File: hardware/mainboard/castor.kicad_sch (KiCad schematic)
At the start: 46 parts, among them J116 OSC, Q1 MMBT3906, U3 TL074, U4 74LVC2G74, U5 MCP6001-OT, U6 TL074

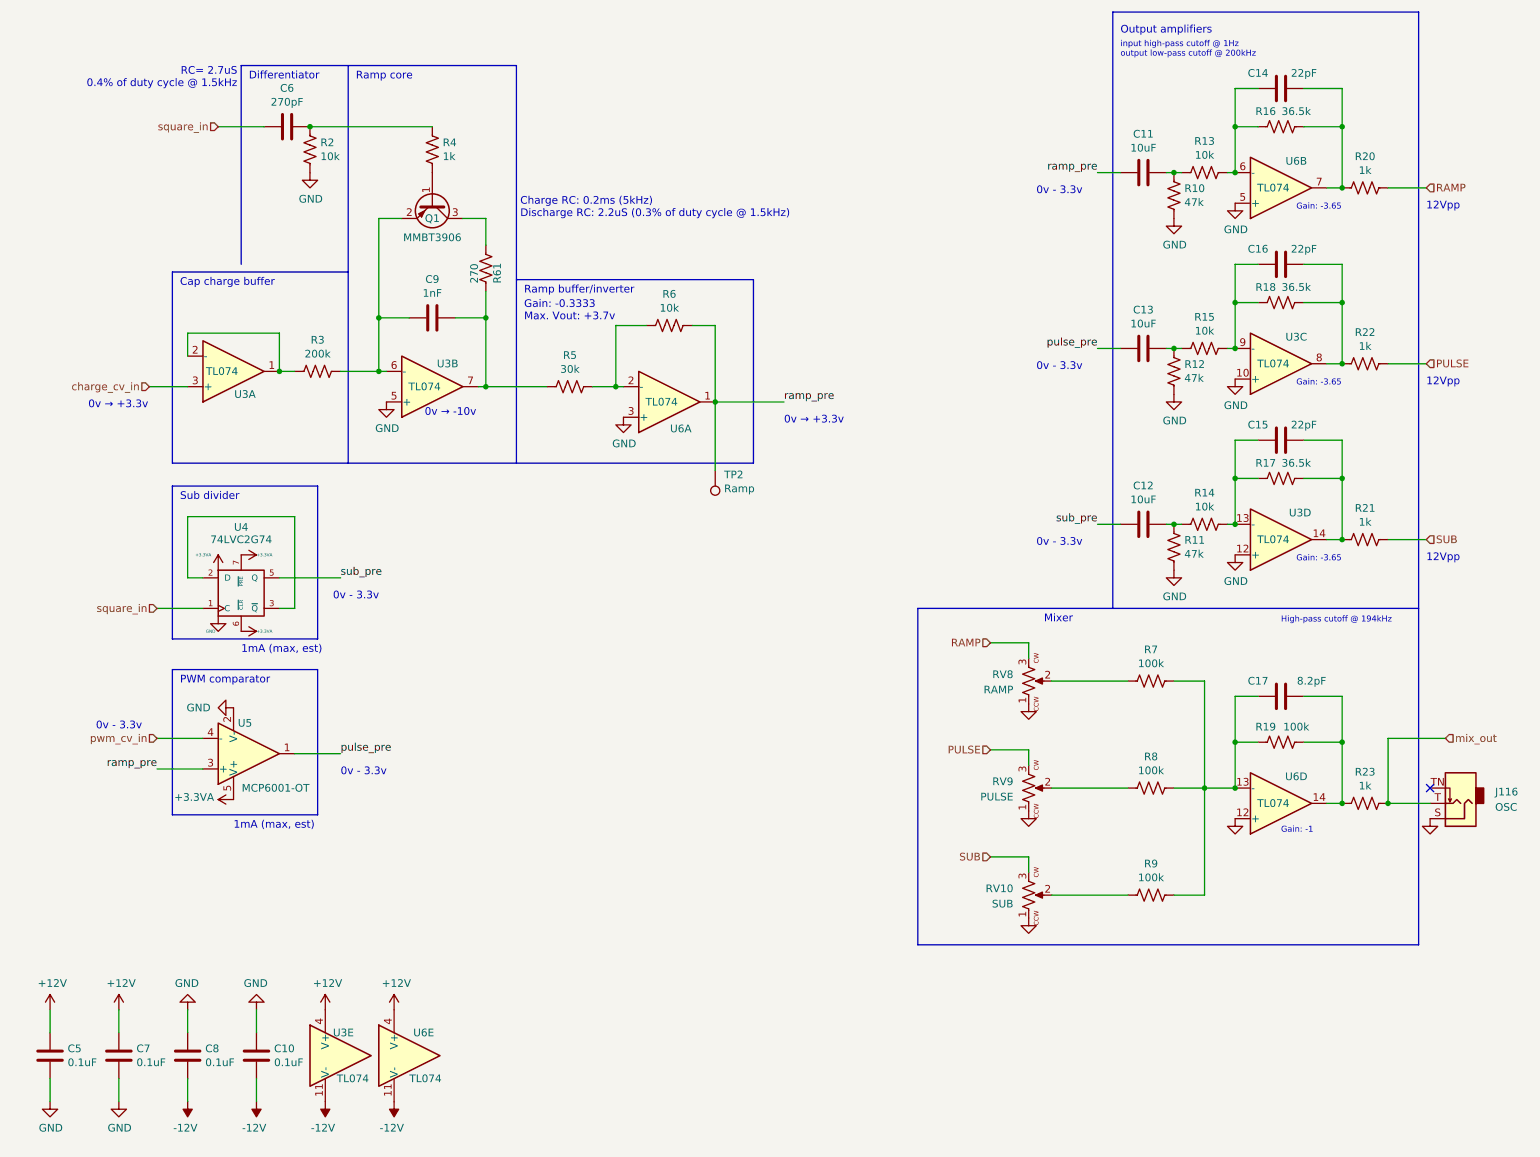
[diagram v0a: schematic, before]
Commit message: Progress on cleaning up the schematics
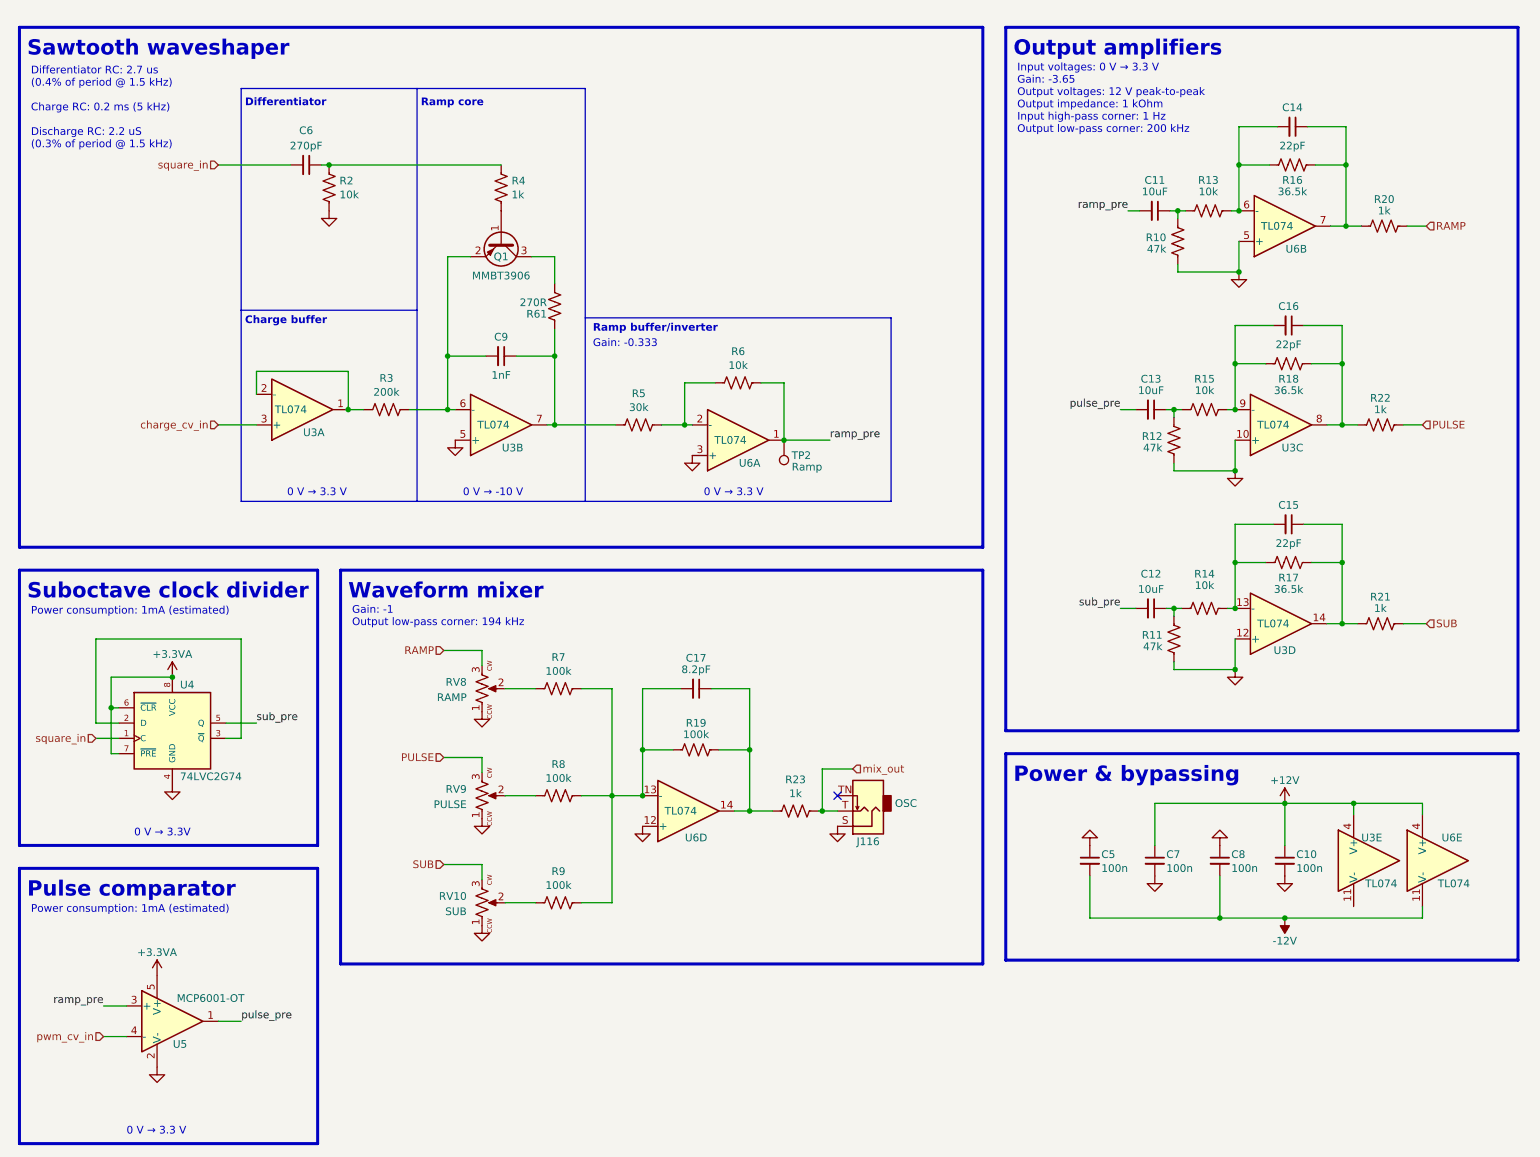
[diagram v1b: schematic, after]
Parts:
- C10, C5, C7, C8: value 0.1uF -> 100n; symbol Device:C -> Device:C_Small
- C11, C12, C13, C14, C15, C16, C17, C6, C9: symbol Device:C -> Device:C_Small
- R61: value 270 -> 270R
- U4: symbol 74xGxx:74LVC2G74 -> winterbloom:74LVC2G74
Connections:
- net +12V: now also C10.1; no longer C5.1
- net -12V: now also C5.2; no longer C10.2, U3.11 (V-)
- net GND: now also C10.2, C5.1; no longer C10.1, C5.2
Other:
- note added: "0 V → -10 V"
- note added: "0 V → 3.3 V"
- note added: "0 V → 3.3V"
- note added: "Charge buffer"
- note added: "Differentiator RC: 2.7 us (0.4% of period @ 1.5 kHz) Charge RC: 0.2 ms (5 kHz) Discharge RC: 2.2 uS (0.3% of period @ 1.5 kHz)"
- note added: "Gain: -0.333"
- note added: "Gain: -1 Output low-pass corner: 194 kHz"
- note added: "Input voltages: 0 V → 3.3 V Gain: -3.65 Output voltages: 12 V peak-to-peak Output impedance: 1 kOhm Input high-pass corner: 1 Hz Output low-pass corner: 200 kHz"
- note added: "Power & bypassing"
- note added: "Power consumption: 1mA (estimated)"
- note added: "Pulse comparator"
- note added: "Sawtooth waveshaper"
- note added: "Suboctave clock divider"
- note added: "Waveform mixer"
- note removed: "0v - 3.3v"
- note removed: "0v → +3.3v"
- note removed: "0v → -10v"
- note removed: "12Vpp"
- note removed: "1mA (max, est)"
- note removed: "Cap charge buffer"
- note removed: "Charge RC: 0.2ms (5kHz) Discharge RC: 2.2uS (0.3% of duty cycle @ 1.5kHz)"
- note removed: "Gain: -0.3333 Max. Vout: +3.7v"
- note removed: "Gain: -1"
- note removed: "Gain: -3.65"
- note removed: "High-pass cutoff @ 194kHz"
- note removed: "Mixer"
- note removed: "PWM comparator"
- note removed: "RC= 2.7uS 0.4% of duty cycle @ 1.5kHz"
- note removed: "Sub divider"
- note removed: "input high-pass cutoff @ 1Hz output low-pass cutoff @ 200kHz"
- moved on the sheet: C10, C11, C12, C13, C14, C15, C16, C17, C5, C6, C7, C8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

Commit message: Fixup some wacked stuff from the schematic cleanup
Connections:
- net +12V: now also C5.1; no longer C10.1
- net -12V: now also C10.2, U3.11 (V-); no longer C5.2
- net GND: now also C10.1, C5.2; no longer C10.2, C5.1
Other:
- moved on the sheet: C10, C5
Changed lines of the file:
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@@
   (junction (at 86.36 78.74) (diameter 0) (color 0 0 0 0)
+  )
+  (junction (at 236.855 163.195) (diameter 0) (color 0 0 0 0)
   )
   (junction (at 234.95 114.3) (diameter 0) (color 0 0 0 0)
@@
     (stroke (width 0.5) (type solid) (color 0 0 0 0))
   )
+  (wire (pts (xy 236.855 163.195) (xy 225.425 163.195))
+    (stroke (width 0) (type default) (color 0 0 0 0))
+  )
   (wire (pts (xy 225.425 144.145) (xy 225.425 151.13))
     (stroke (width 0) (type default) (color 0 0 0 0))
@@
     (stroke (width 0) (type default) (color 0 0 0 0))
   )
-  (wire (pts (xy 248.285 163.195) (xy 225.425 163.195))
+  (wire (pts (xy 248.285 163.195) (xy 236.855 163.195))
     (stroke (width 0) (type default) (color 0 0 0 0))
   )
@@
   )
   (wire (pts (xy 207.01 78.74) (xy 207.01 80.01))
+    (stroke (width 0) (type default) (color 0 0 0 0))
+  )
+  (wire (pts (xy 236.855 161.29) (xy 236.855 163.195))
     (stroke (width 0) (type default) (color 0 0 0 0))
   )
@@
     (pin "1")
   )
+  (symbol (lib_id "Device:C_Small") (at 193.04 153.67 0) (unit 1)
+    (in_bom yes) (on_board yes)
+    (property "Reference" "C10" (id 0) (at 194.945 152.4 0)
+      (effects (font (size 1.27 1.27)) (justify left))
+    )
+    (property "Value" "100n" (id 1) (at 194.945 154.94 0)
+      (effects (font (size 1.27 1.27)) (justify left))
+    )
+    (property "Footprint" "Capacitor_SMD:C_0402_1005Metric_Pad0.74x0.62mm_HandSolder" (id 2) (at 194.0052 157.48 0)
+      (effects (font (size 1.27 1.27)) hide)
+    )
+    (property "Datasheet" "~" (id 3) (at 193.04 153.67 0)
+      (effects (font (size 1.27 1.27)) hide)
+    )
+    (property "finalized" "yes" (id 4) (at 193.04 153.67 0)
+      (effects (font (size 1.27 1.27)) hide)
+    )
+    (property "mpn" "MF-CAP-0603-0.1uF" (id 5) (at 193.04 153.67 0)
+      (effects (font (size 1.27 1.27)) hide)
+    )
+    (property "mpn specs" "10%, 25v" (id 6) (at 193.04 153.67 0)
+      (effects (font (size 1.27 1.27)) hide)
+    )
+    (property "mpn alt" "GCM188R91E104KA37D" (id 7) (at 193.04 153.67 0)
+      (effects (font (size 1.27 1.27)) hide)
+    )
+    (property "Reqs" "bypass, 16v+" (id 8) (at 193.04 153.67 0)
+      (effects (font (size 1.27 1.27)) hide)
+    )
+    (pin "1")
+    (pin "2")
+  )
+  (symbol (lib_id "Device:C_Small") (at 214.63 153.67 0) (unit 1)
+    (in_bom yes) (on_board yes)
+    (property "Reference" "C8" (id 0) (at 216.535 152.4 0)
+      (effects (font (size 1.27 1.27)) (justify left))
+    )
+    (property "Value" "100n" (id 1) (at 216.535 154.94 0)
+      (effects (font (size 1.27 1.27)) (justify left))
+    )
+    (property "Footprint" "Capacitor_SMD:C_0402_1005Metric_Pad0.74x0.62mm_HandSolder" (id 2) (at 215.5952 157.48 0)
+      (effects (font (size 1.27 1.27)) hide)
+    )
+    (property "Datasheet" "~" (id 3) (at 214.63 153.67 0)
+      (effects (font (size 1.27 1.27)) hide)
+    )
+    (property "finalized" "yes" (id 4) (at 214.63 153.67 0)
+      (effects (font (size 1.27 1.27)) hide)
+    )
+    (property "mpn" "MF-CAP-0603-0.1uF" (id 5) (at 214.63 153.67 0)
+      (effects (font (size 1.27 1.27)) hide)
+    )
+    (property "mpn specs" "10%, 25v" (id 6) (at 214.63 153.67 0)
+      (effects (font (size 1.27 1.27)) hide)
+    )
+    (property "mpn alt" "GCM188R91E104KA37D" (id 7) (at 214.63 153.67 0)
+      (effects (font (size 1.27 1.27)) hide)
+    )
+    (property "Reqs" "bypass, 16v+" (id 8) (at 214.63 153.67 0)
+      (effects (font (size 1.27 1.27)) hide)
+    )
+    (pin "1")
+    (pin "2")
+  )
+  (symbol (lib_id "Device:C_Small") (at 203.835 153.67 0) (unit 1)
+    (in_bom yes) (on_board yes)
+    (property "Reference" "C7" (id 0) (at 205.74 152.4 0)
+      (effects (font (size 1.27 1.27)) (justify left))
+    )
+    (property "Value" "100n" (id 1) (at 205.74 154.94 0)
+      (effects (font (size 1.27 1.27)) (justify left))
+    )
+    (property "Footprint" "Capacitor_SMD:C_0402_1005Metric_Pad0.74x0.62mm_HandSolder" (id 2) (at 204.8002 157.48 0)
+      (effects (font (size 1.27 1.27)) hide)
+    )
+    (property "Datasheet" "~" (id 3) (at 203.835 153.67 0)
+      (effects (font (size 1.27 1.27)) hide)
+    )
+    (property "finalized" "yes" (id 4) (at 203.835 153.67 0)
+      (effects (font (size 1.27 1.27)) hide)
+    )
+    (property "mpn" "MF-CAP-0603-0.1uF" (id 5) (at 203.835 153.67 0)
+      (effects (font (size 1.27 1.27)) hide)
+    )
+    (property "mpn specs" "10%, 25v" (id 6) (at 203.835 153.67 0)
+      (effects (font (size 1.27 1.27)) hide)
+    )
+    (property "mpn alt" "GCM188R91E104KA37D" (id 7) (at 203.835 153.67 0)
+      (effects (font (size 1.27 1.27)) hide)
+    )
+    (property "Reqs" "bypass, 16v+" (id 8) (at 203.835 153.67 0)
+      (effects (font (size 1.27 1.27)) hide)
+    )
+    (pin "1")
+    (pin "2")
+  )
   (symbol (lib_id "Device:C_Small") (at 225.425 153.67 0) (unit 1)
     (in_bom yes) (on_board yes)
-    (property "Reference" "C10" (id 0) (at 227.33 152.6286 0)
+    (property "Reference" "C5" (id 0) (at 227.33 152.4 0)
       (effects (font (size 1.27 1.27)) (justify left))
     )
@@
     )
     (property "Reqs" "bypass, 16v+" (id 8) (at 225.425 153.67 0)
-      (effects (font (size 1.27 1.27)) hide)
-    )
-    (pin "1")
-    (pin "2")
-  )
-  (symbol (lib_id "Device:C_Small") (at 214.63 153.67 0) (unit 1)
-    (in_bom yes) (on_board yes)
-    (property "Reference" "C8" (id 0) (at 216.535 152.6286 0)
-      (effects (font (size 1.27 1.27)) (justify left))
-    )
-    (property "Value" "100n" (id 1) (at 216.535 154.94 0)
-      (effects (font (size 1.27 1.27)) (justify left))
-    )
-    (property "Footprint" "Capacitor_SMD:C_0402_1005Metric_Pad0.74x0.62mm_HandSolder" (id 2) (at 215.5952 157.48 0)
-      (effects (font (size 1.27 1.27)) hide)
-    )
-    (property "Datasheet" "~" (id 3) (at 214.63 153.67 0)
-      (effects (font (size 1.27 1.27)) hide)
-    )
-    (property "finalized" "yes" (id 4) (at 214.63 153.67 0)
-      (effects (font (size 1.27 1.27)) hide)
-    )
-    (property "mpn" "MF-CAP-0603-0.1uF" (id 5) (at 214.63 153.67 0)
-      (effects (font (size 1.27 1.27)) hide)
-    )
-    (property "mpn specs" "10%, 25v" (id 6) (at 214.63 153.67 0)
-      (effects (font (size 1.27 1.27)) hide)
-    )
-    (property "mpn alt" "GCM188R91E104KA37D" (id 7) (at 214.63 153.67 0)
-      (effects (font (size 1.27 1.27)) hide)
-    )
-    (property "Reqs" "bypass, 16v+" (id 8) (at 214.63 153.67 0)
-      (effects (font (size 1.27 1.27)) hide)
-    )
-    (pin "1")
-    (pin "2")
-  )
-  (symbol (lib_id "Device:C_Small") (at 203.835 153.67 0) (unit 1)
-    (in_bom yes) (on_board yes)
-    (property "Reference" "C7" (id 0) (at 205.74 152.6286 0)
-      (effects (font (size 1.27 1.27)) (justify left))
-    )
-    (property "Value" "100n" (id 1) (at 205.74 154.94 0)
-      (effects (font (size 1.27 1.27)) (justify left))
-    )
-    (property "Footprint" "Capacitor_SMD:C_0402_1005Metric_Pad0.74x0.62mm_HandSolder" (id 2) (at 204.8002 157.48 0)
-      (effects (font (size 1.27 1.27)) hide)
-    )
-    (property "Datasheet" "~" (id 3) (at 203.835 153.67 0)
-      (effects (font (size 1.27 1.27)) hide)
-    )
-    (property "finalized" "yes" (id 4) (at 203.835 153.67 0)
-      (effects (font (size 1.27 1.27)) hide)
-    )
-    (property "mpn" "MF-CAP-0603-0.1uF" (id 5) (at 203.835 153.67 0)
-      (effects (font (size 1.27 1.27)) hide)
-    )
-    (property "mpn specs" "10%, 25v" (id 6) (at 203.835 153.67 0)
-      (effects (font (size 1.27 1.27)) hide)
-    )
-    (property "mpn alt" "GCM188R91E104KA37D" (id 7) (at 203.835 153.67 0)
-      (effects (font (size 1.27 1.27)) hide)
-    )
-    (property "Reqs" "bypass, 16v+" (id 8) (at 203.835 153.67 0)
-      (effects (font (size 1.27 1.27)) hide)
-    )
-    (pin "1")
-    (pin "2")
-  )
-  (symbol (lib_id "Device:C_Small") (at 193.04 153.67 0) (unit 1)
-    (in_bom yes) (on_board yes)
-    (property "Reference" "C5" (id 0) (at 194.945 152.6286 0)
-      (effects (font (size 1.27 1.27)) (justify left))
-    )
-    (property "Value" "100n" (id 1) (at 194.945 154.94 0)
-      (effects (font (size 1.27 1.27)) (justify left))
-    )
-    (property "Footprint" "Capacitor_SMD:C_0402_1005Metric_Pad0.74x0.62mm_HandSolder" (id 2) (at 194.0052 157.48 0)
-      (effects (font (size 1.27 1.27)) hide)
-    )
-    (property "Datasheet" "~" (id 3) (at 193.04 153.67 0)
-      (effects (font (size 1.27 1.27)) hide)
-    )
-    (property "finalized" "yes" (id 4) (at 193.04 153.67 0)
-      (effects (font (size 1.27 1.27)) hide)
-    )
-    (property "mpn" "MF-CAP-0603-0.1uF" (id 5) (at 193.04 153.67 0)
-      (effects (font (size 1.27 1.27)) hide)
-    )
-    (property "mpn specs" "10%, 25v" (id 6) (at 193.04 153.67 0)
-      (effects (font (size 1.27 1.27)) hide)
-    )
-    (property "mpn alt" "GCM188R91E104KA37D" (id 7) (at 193.04 153.67 0)
-      (effects (font (size 1.27 1.27)) hide)
-    )
-    (property "Reqs" "bypass, 16v+" (id 8) (at 193.04 153.67 0)
       (effects (font (size 1.27 1.27)) hide)
     )
@@
   (symbol (lib_id "power:GND") (at 203.835 156.21 0) (unit 1)
     (in_bom yes) (on_board yes)
-    (property "Reference" "#PWR?" (id 0) (at 203.835 162.56 0)
+    (property "Reference" "#PWR0101" (id 0) (at 203.835 162.56 0)
       (effects (font (size 1.27 1.27)) hide)
     )
@@
   (symbol (lib_id "power:GND") (at 214.63 151.13 180) (unit 1)
     (in_bom yes) (on_board yes)
-    (property "Reference" "#PWR?" (id 0) (at 214.63 144.78 0)
+    (property "Reference" "#PWR0111" (id 0) (at 214.63 144.78 0)
       (effects (font (size 1.27 1.27)) hide)
     )
@@
   (symbol (lib_id "power:GND") (at 225.425 156.21 0) (unit 1)
     (in_bom yes) (on_board yes)
-    (property "Reference" "#PWR?" (id 0) (at 225.425 162.56 0)
-      (effects (font (size 1.27 1.27)) hide)
-    )
+    (property "Reference" "#PWR0102" (id 0) (at 225.425 162.56 0)
+      (effects (font (size 1.27 1.27)) hide)
+    )
